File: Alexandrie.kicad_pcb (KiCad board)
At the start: 2 copper layers, 100 x 100 mm, 47 parts, among them J1 , J11 , J2 , J3 , J4 , J5 , J6 , J7 , J8 , U1 74HCT04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

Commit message: Readme cleaning, add 2 3D pictures
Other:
- board text added: "Gnd +12V Gnd 6m 12/10m 17/15m 6m 30/20m 40m 80m 160m"
- board text added: "Gnd +12V HPF_ByPass Gnd 6mLNA 1.5HPF 6.5HPF 9.5HPF 13HPF 20HPF Att2 Att1 TX_RX_RLY"
- board text removed: "160m 80m 40m 30/20m 17/15m 12/10m 6m Gnd +12V Gnd"
- board text removed: "TX_RX_RLY Att1 Att2 20HPF 13HPF 9.5HPF 6.5HPF 1.5HPF 6mLNA Gnd HPF_ByPass +12V Gnd"
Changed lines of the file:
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@@
     (links 162)
     (no_connects 0)
-    (area 86.0088 42.525 191.21726 143.575)
+    (area 88.924999 42.924999 189.075001 143.075001)
     (thickness 1.6)
     (drawings 15)
@@
     (effects (font (size 1.5 1.5) (thickness 0.3)) (justify left mirror))
   )
-  (gr_text "160m\n80m\n40m\n30/20m\n17/15m\n12/10m\n6m\nGnd\n+12V\nGnd\n" (at 183 77 180) (layer B.SilkS)
-    (effects (font (size 1.5 1.5) (thickness 0.3)) (justify right mirror))
-  )
-  (gr_text "TX_RX_RLY\nAtt1\nAtt2\n20HPF\n13HPF\n9.5HPF\n6.5HPF\n1.5HPF\n6mLNA\nGnd\nHPF_ByPass\n+12V\nGnd" (at 183 109 180) (layer B.SilkS)
-    (effects (font (size 1.5 1.5) (thickness 0.3)) (justify right mirror))
+  (gr_text "Gnd\n+12V\nGnd\n6m\n12/10m\n17/15m\n6m 30/20m\n40m\n80m\n160m\n" (at 183.25 77.5) (layer B.SilkS)
+    (effects (font (size 1.5 1.5) (thickness 0.3)) (justify left mirror))
+  )
+  (gr_text "Gnd\n+12V\nHPF_ByPass\nGnd\n6mLNA\n1.5HPF\n6.5HPF\n9.5HPF\n13HPF\n20HPF\nAtt2\nAtt1\nTX_RX_RLY" (at 183.25 108.75) (layer B.SilkS)
+    (effects (font (size 1.5 1.5) (thickness 0.3)) (justify left mirror))
   )
   (segment (start 116.7 91.19) (end 115.06 91.19) (width 0.6) (layer F.Cu) (net 1))

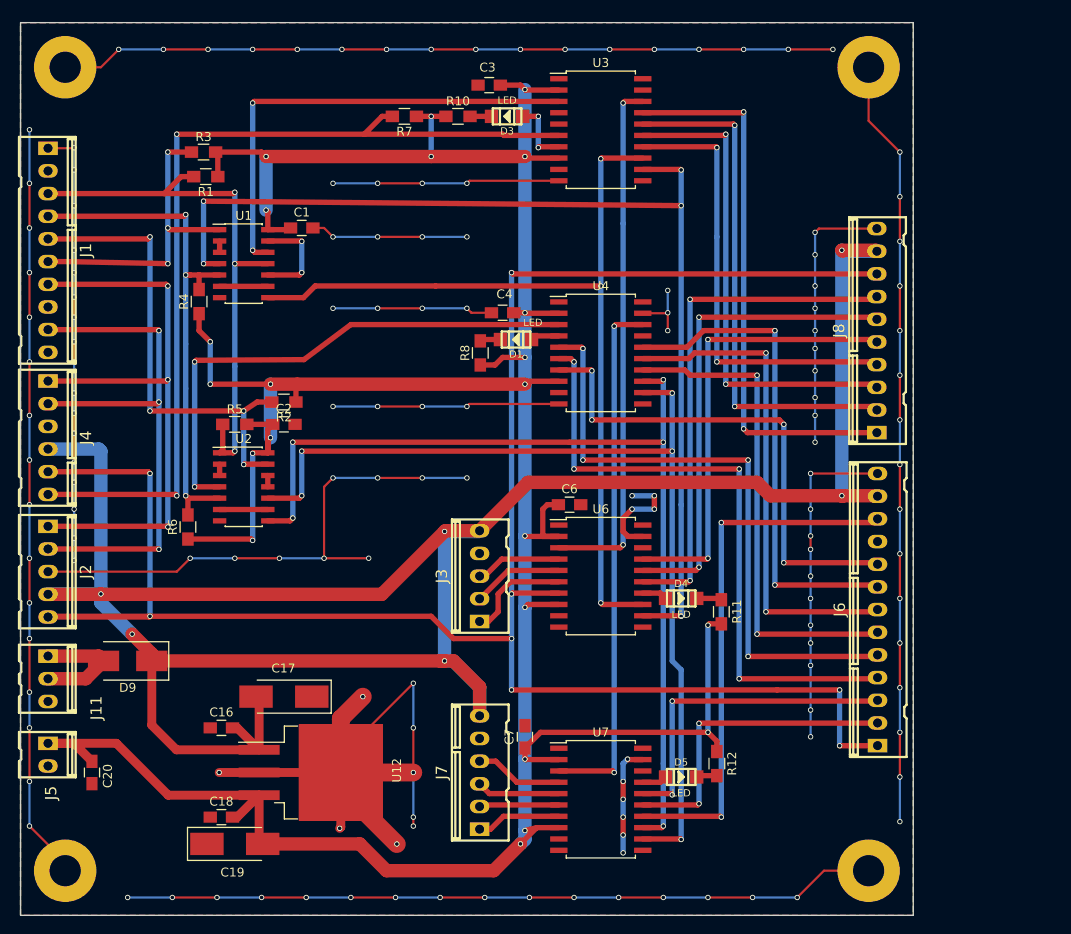
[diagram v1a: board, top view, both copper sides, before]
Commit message: new footprint for drivers
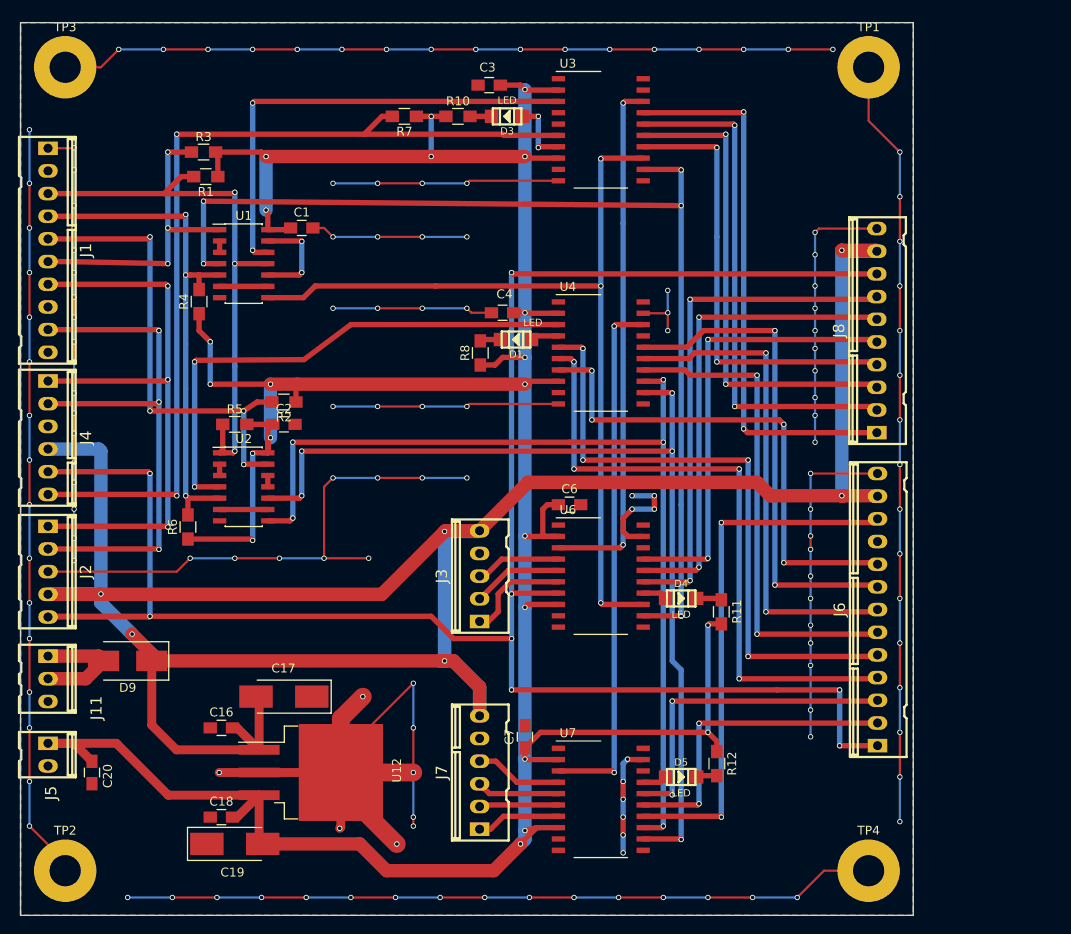
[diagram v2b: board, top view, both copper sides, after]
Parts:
- J1, J8: value (none) -> kk_10
- J11: value (none) -> CONN_01X03
- J2, J3: value (none) -> kk_5
- J4, J7: value (none) -> CONN_01X06
- J5: value (none) -> CONN_01X02
- J6: value (none) -> CONN_01X13
- TP1, TP2, TP3, TP4: renamed from  ; value (none) -> TEST
- U3, U4, U6, U7: footprint Housings_SOIC:SOIC-20W_7.5x12.8mm_Pitch1.27mm -> Housings_SOIC:SO-20_12.8x7.5mm_Pitch1.27mm

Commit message: minor changes, BOM added
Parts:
- moved R10 2.75 mm to (137.9, 56.2)
- moved D3 2.75 mm to (143.5, 56.2)
- moved R7 2.75 mm to (132.0, 56.2)
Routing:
- net +12V: track 271.3 -> 265.4 mm, vias 6 -> 9
- net Net-(D3-Pad1): track 7.59 -> 4.27 mm, vias 2 -> 0
- net +5V: track 381.4 -> 382.8 mm, vias 22 -> 21
- net Net-(U1-Pad4): track 120.9 -> 120.4 mm
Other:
- board text added: "12V In"
- board text added: "5V Out"
- board text added: "Alex Input"
- board text added: "Alexiares control board Ἀλεξάνδρεια (Alexandrie)"
- board text added: "And on the pedestal these words appear: "My name is Ozymandias, king of kings: Look on my works, Ye Mighty, and despair!""
- board text added: "RX_Ant"
- board text added: "Schematic KE9H/ VK6APH Drawing f6itu"
- board text added: "TX_Ant"
- board text added: "To Alex HPF"
- board text added: "To Alex LPF"
- board text added: "To Mentor Ctrl Brd"
- board text added: "To VSWR/PS/TX-RX Board"
